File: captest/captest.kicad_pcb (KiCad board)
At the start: 2 copper layers, 36.2 x 36.2 mm, 12 parts, among them IC1 ATTINY861-P, P1 CONN_2, P2 CONN_6, P3 CONN_3X2

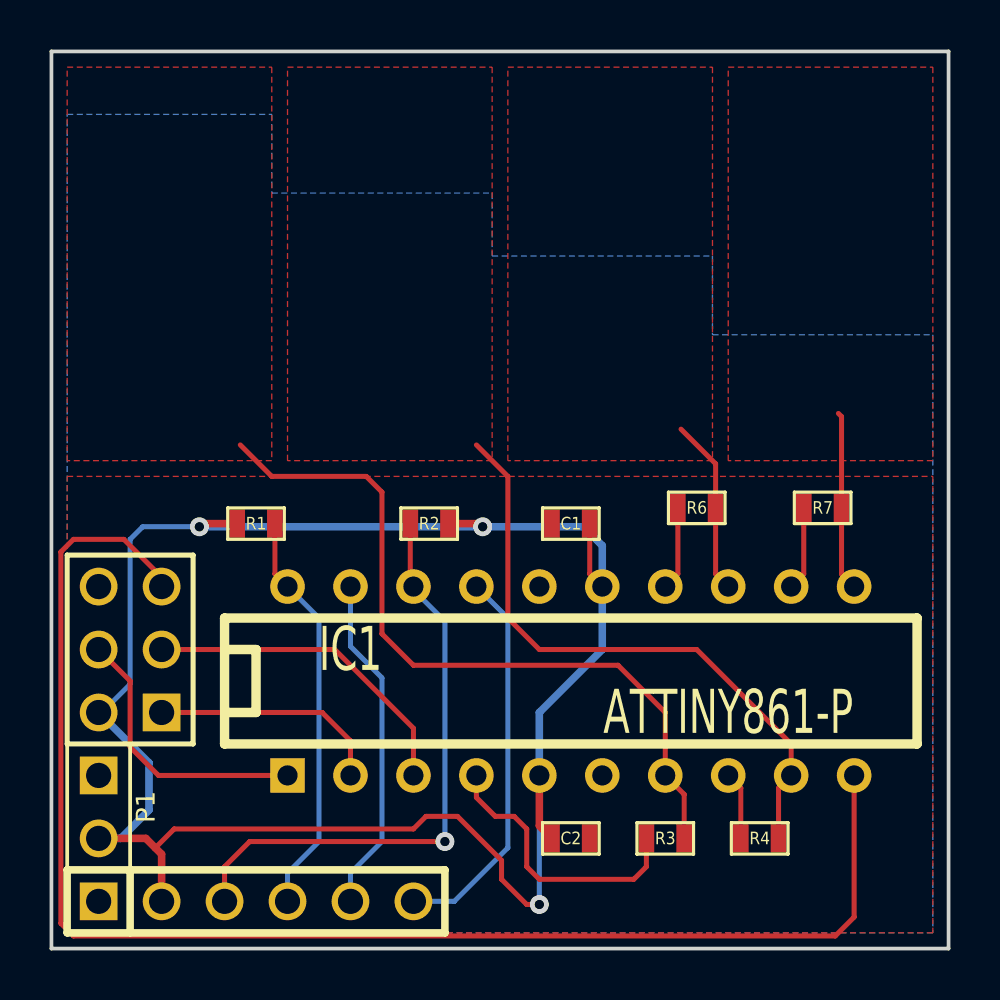
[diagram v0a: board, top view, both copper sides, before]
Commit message: Captest silkscreen adjustments
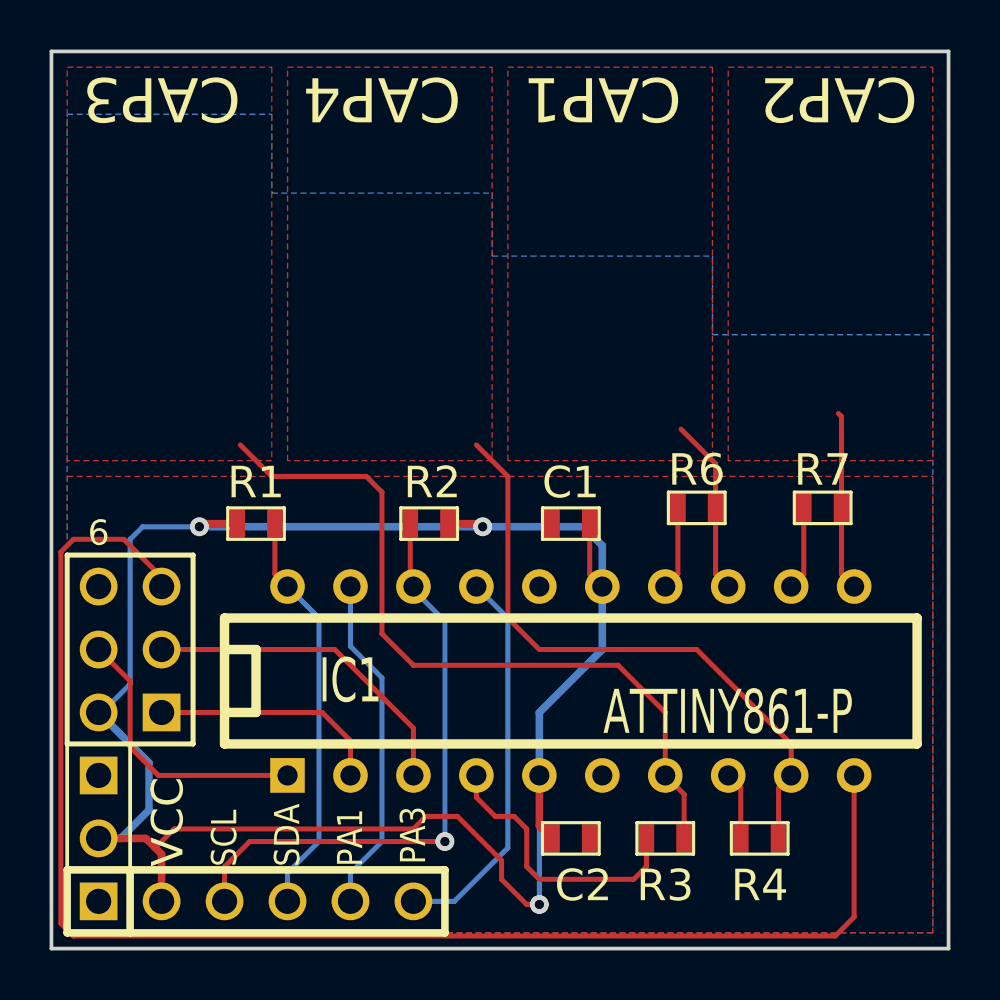
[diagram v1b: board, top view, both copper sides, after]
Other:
- board text added: "6"
- board text added: "CAP1"
- board text added: "CAP2"
- board text added: "CAP3"
- board text added: "CAP4"
- board text added: "Capacitive touch sensor test board"
- board text added: "PA1"
- board text added: "PA3"
- board text added: "SCL"
- board text added: "SDA"
- board text added: "VCC"

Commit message: Captest updates
* Change to SOIC-20 version of ATtiny861
* Add filtering caps on sense pins
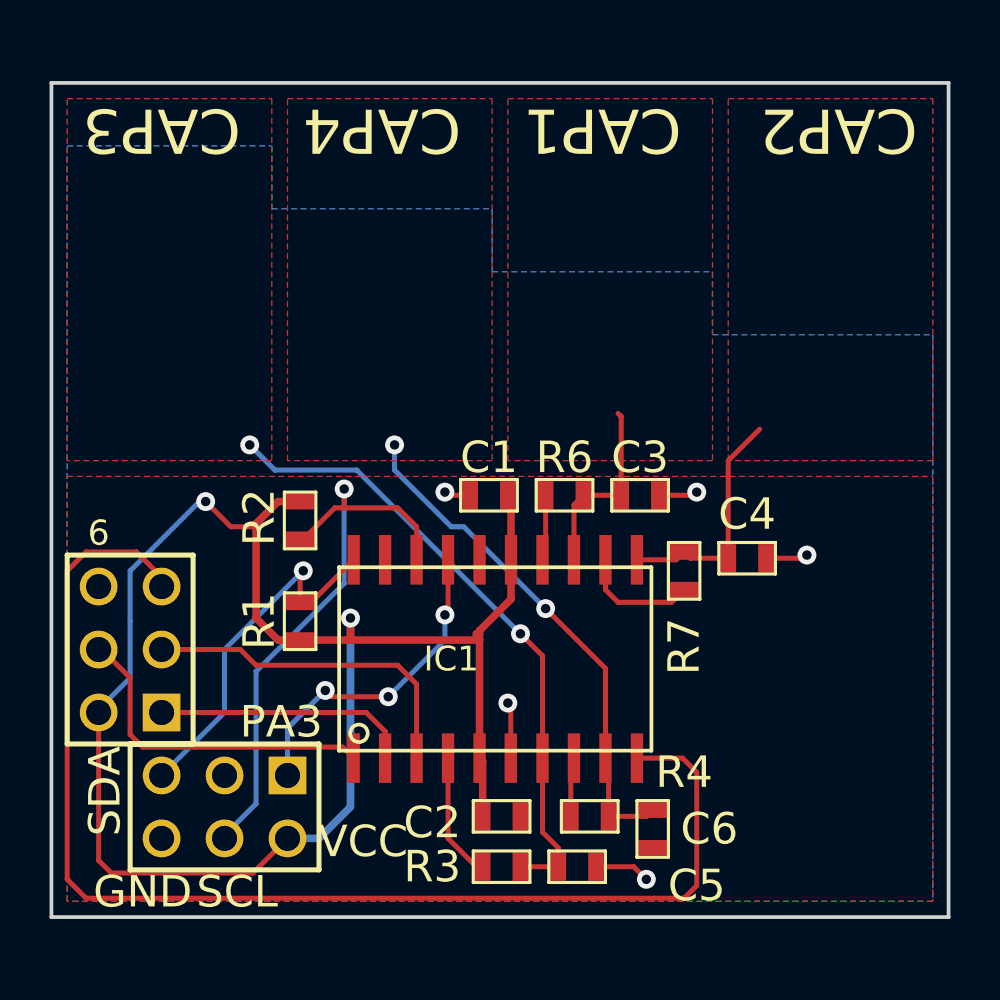
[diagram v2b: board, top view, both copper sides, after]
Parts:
- removed P2: CONN_6, PIN_ARRAY-6X1
- added C3: C, SM0603, F.Cu at (162.8, 90.9)
- added C4: C, SM0603, F.Cu at (167.1, 93.5)
- added C5: C, SM0603, F.Cu at (160.3, 105.9)
- added C6: C, SM0603, F.Cu at (163.3, 104.4)
- IC1: footprint DIP-20__300 -> SOIC20-7.4MM
- P1: value CONN_2 -> CONN_3X2; footprint PIN_ARRAY_2X1 -> pin_array_3x2
- moved R4 6.92 mm to (160.8, 103.9)
- moved R3 6.70 mm to (157.2, 105.9)
- moved R7 6.14 mm to (164.6, 94.0), turned to 90 degrees
- moved R6 5.36 mm to (159.8, 90.9)
- moved R2 5.21 mm to (149.1, 91.9), turned to 270 degrees
- moved P1 5.08 mm to (146.1, 103.5), turned to 180 degrees
- moved R1 4.32 mm to (149.1, 96.0), turned to 90 degrees
- moved C1 3.49 mm to (156.7, 90.9)
- moved IC1 3.18 mm to (157.0, 97.5)
- moved C2 2.93 mm to (157.2, 103.9)
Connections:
- IC1 pad 19: /PA1 -> (no net)
- P1 pad 1: GND -> /PA3
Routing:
- net /PA1: track 13.8 -> 0.00 mm
- net VCC: track 81.2 -> 68.5 mm, vias 3 -> 2
- net GND: track 0.00 -> 8.86 mm, vias 0 -> 5
- net /nRESET: track 58.5 -> 50.5 mm
- net N-000006: track 11.4 -> 5.11 mm
- net /CAP3: track 30.4 -> 25.6 mm, vias 0 -> 2
- net /CAP4: track 25.1 -> 20.7 mm, vias 0 -> 2
- net /PA3: track 15.8 -> 13.2 mm, vias 0 -> 3
- net /CAP2: track 7.25 -> 9.65 mm
- net /MOSI: track 11.3 -> 13.4 mm
- net /SDA: track 16.5 -> 14.8 mm, vias 0 -> 1
- net N-0000013: track 3.39 -> 4.80 mm
- net /MISO: track 9.49 -> 10.4 mm
- net N-0000014: track 3.39 -> 2.66 mm
- net /CAP1: track 7.14 -> 7.64 mm
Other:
- board size 36.2 x 36.2 mm -> 36.2 x 33.7 mm
- board text added: "GND"
- board text removed: "PA1"

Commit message: Captest update with TSSOP and more density
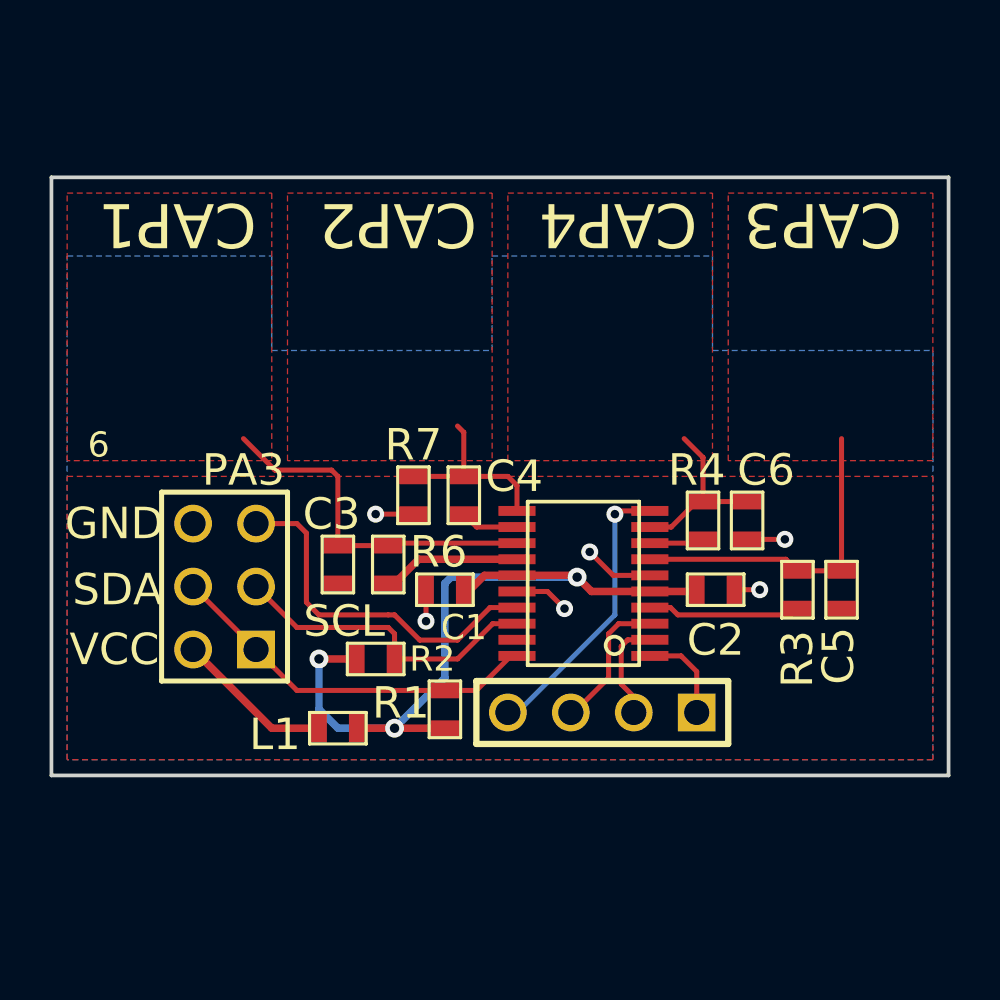
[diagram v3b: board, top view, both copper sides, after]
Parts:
- removed P3: CONN_3X2, pin_array_3x2
- added L1: INDUCTOR, SM0603, F.Cu at (150.6, 100.3)
- added P2: CONN_4, PIN_ARRAY_4x1, F.Cu at (161.3, 99.7)
- IC1: footprint SOIC20-7.4MM -> TSSOP20-4.5MM
- moved R3 16.4 mm to (169.2, 94.7), turned to 90 degrees
- moved C5 15.5 mm to (170.9, 94.7), turned to 270 degrees
- moved C4 13.7 mm to (153.7, 90.9), turned to 270 degrees
- moved C6 13.0 mm to (167.1, 91.9)
- moved R4 12.8 mm to (165.4, 91.9), turned to 90 degrees
- moved C2 12.6 mm to (165.9, 94.7)
- moved C3 12.5 mm to (150.6, 93.7), turned to 270 degrees
- moved R7 9.40 mm to (155.7, 90.9)
- moved P1 8.89 mm to (146.1, 94.6), turned to 90 degrees
- moved R6 7.64 mm to (152.7, 93.7), turned to 90 degrees
- moved R1 6.84 mm to (154.9, 99.6)
- moved R2 6.37 mm to (152.1, 97.5), turned to 0 degrees
- moved IC1 4.68 mm to (160.5, 94.5), turned to 90 degrees
- moved C1 4.20 mm to (154.9, 94.7)
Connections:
- P1 pad 1: /PA3 -> /SDA
- P1 pad 2: VCC -> /PWR
- P1 pad 3: (no net) -> /SCL
- P1 pad 4: /SCL -> /SDA
- P1 pad 5: /SDA -> /PA3
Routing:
- net /nRESET: track 50.5 -> 11.5 mm, vias 0 -> 1
- net VCC: track 68.5 -> 32.6 mm, vias 2 -> 3
- net /CAP4: track 20.7 -> 7.21 mm, vias 2 -> 0
- net /CAP3: track 25.6 -> 13.3 mm, vias 2 -> 0
- net /SCL: track 23.7 -> 12.9 mm, vias 1 -> 0
- net /MOSI: track 13.4 -> 3.80 mm
- net /SCK: track 13.8 -> 5.71 mm
- net /CAP1: track 7.64 -> 14.5 mm
- net /PWR: track 0.00 -> 6.40 mm
- net /MISO: track 10.4 -> 4.14 mm
- net N-000006: track 2.66 -> 5.60 mm
- net N-000002: track 4.80 -> 2.36 mm
- net /CAP2: track 9.65 -> 7.49 mm
- net GND: track 8.86 -> 10.4 mm, vias 5 -> 6
- net /PA3: track 13.2 -> 14.7 mm, vias 3 -> 0
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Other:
- board size 36.2 x 33.7 mm -> 36.2 x 24.1 mm
- net class Default: via_dia 0.762 -> 0.6858; via_drill 0.508 -> 0.381
- board text added: "MISO"
- board text added: "MOSI"
- board text added: "RESET"
- board text added: "SCK"

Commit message: Optimize captest layout
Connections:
- IC1 pad 19: (no net) -> GND
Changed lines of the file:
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@@
 (kicad_pcb (version 3) (host pcbnew "(2013-feb-26)-testing")
   (general
-    (links 37)
+    (links 38)
     (no_connects 0)
     (area 138.989999 78.029999 175.335001 103.0986)
@@
     (user_trace_width 0.2032)
     (trace_clearance 0.2032)
-    (zone_clearance 0.2032)
+    (zone_clearance 0.254)
     (zone_45_only no)
     (trace_min 0.1524)
@@
   (net 14 N-000001)
   (net 15 N-000002)
-  (net 16 N-000006)
-  (net 17 N-000007)
+  (net 16 N-000004)
+  (net 17 N-000005)
   (net 18 VCC)
   (net_class Default "This is the default net class."
@@
     (add_net N-000001)
     (add_net N-000002)
-    (add_net N-000006)
-    (add_net N-000007)
+    (add_net N-000004)
+    (add_net N-000005)
   )
   (net_class power ""
@@
     (pad 1 smd rect (at -0.762 0 90) (size 0.635 1.143)
       (layers F.Cu F.Paste F.Mask)
-      (net 16 N-000006)
+      (net 16 N-000004)
     )
     (pad 2 smd rect (at 0.762 0 90) (size 0.635 1.143)
@@
     (pad 1 smd rect (at -0.762 0 90) (size 0.635 1.143)
       (layers F.Cu F.Paste F.Mask)
-      (net 15 N-000002)
+      (net 17 N-000005)
     )
     (pad 2 smd rect (at 0.762 0 90) (size 0.635 1.143)
@@
     (pad 1 smd rect (at -0.762 0 90) (size 0.635 1.143)
       (layers F.Cu F.Paste F.Mask)
-      (net 17 N-000007)
+      (net 15 N-000002)
     )
     (pad 2 smd rect (at 0.762 0 90) (size 0.635 1.143)
@@
     (pad 8 smd rect (at 1.625 2.68 90) (size 0.4 1.5)
       (layers F.Cu F.Paste F.Mask)
-      (net 17 N-000007)
+      (net 15 N-000002)
       (clearance 0.125)
     )
@@
     (pad 12 smd rect (at 2.275 -2.68 90) (size 0.4 1.5)
       (layers F.Cu F.Paste F.Mask)
-      (net 15 N-000002)
+      (net 17 N-000005)
       (clearance 0.125)
     )
@@
     (pad 14 smd rect (at 0.975 -2.68 90) (size 0.4 1.5)
       (layers F.Cu F.Paste F.Mask)
-      (net 16 N-000006)
+      (net 16 N-000004)
       (clearance 0.125)
     )
@@
     (pad 19 smd rect (at -2.275 -2.68 90) (size 0.4 1.5)
       (layers F.Cu F.Paste F.Mask)
+      (net 13 GND)
       (clearance 0.125)
     )
@@
   (segment (start 164.338 95.758) (end 168.91 95.758) (width 0.2032) (layer F.Cu) (net 14))
   (segment (start 164.043 95.463) (end 164.338 95.758) (width 0.2032) (layer F.Cu) (net 14))
-  (segment (start 157.848 92.213) (end 156.221 92.213) (width 0.2032) (layer F.Cu) (net 15))
-  (segment (start 156.221 92.213) (end 155.702 91.694) (width 0.2032) (layer F.Cu) (net 15))
+  (segment (start 163.208 92.863) (end 165.201 92.863) (width 0.2032) (layer F.Cu) (net 15))
+  (segment (start 165.201 92.863) (end 165.354 92.71) (width 0.2032) (layer F.Cu) (net 15))
   (segment (start 152.654 94.488) (end 152.908 94.488) (width 0.3048) (layer F.Cu) (net 16))
   (segment (start 153.883 93.513) (end 157.848 93.513) (width 0.3048) (layer F.Cu) (net 16))
   (segment (start 152.908 94.488) (end 153.883 93.513) (width 0.3048) (layer F.Cu) (net 16))
-  (segment (start 163.208 92.863) (end 165.201 92.863) (width 0.2032) (layer F.Cu) (net 17))
-  (segment (start 165.201 92.863) (end 165.354 92.71) (width 0.2032) (layer F.Cu) (net 17))
+  (segment (start 157.848 92.213) (end 156.221 92.213) (width 0.2032) (layer F.Cu) (net 17))
+  (segment (start 156.221 92.213) (end 155.702 91.694) (width 0.2032) (layer F.Cu) (net 17))
   (segment (start 151.384 97.536) (end 149.86 97.536) (width 0.3048) (layer F.Cu) (net 18))
   (segment (start 150.622 100.33) (end 152.908 100.33) (width 0.3048) (layer B.Cu) (net 18))
@@
     )
   )
-  (zone (net 3) (net_name /CAP3) (layer F.Cu) (hatch edge 0.508)
+  (zone (net 1) (net_name /CAP1) (layer F.Cu) (hatch edge 0.508)
     (connect_pads (clearance 0.254))
     (min_thickness 0.254)
@@
     )
   )
-  (zone (net 4) (net_name /CAP4) (layer F.Cu) (hatch edge 0.508)
+  (zone (net 2) (net_name /CAP2) (layer F.Cu) (hatch edge 0.508)
     (connect_pads (clearance 0.254))
     (min_thickness 0.254)
@@
     )
   )
-  (zone (net 1) (net_name /CAP1) (layer F.Cu) (hatch edge 0.508)
+  (zone (net 4) (net_name /CAP4) (layer F.Cu) (hatch edge 0.508)
     (connect_pads (clearance 0.254))
     (min_thickness 0.254)
@@
     )
   )
-  (zone (net 2) (net_name /CAP2) (layer F.Cu) (hatch edge 0.508)
+  (zone (net 3) (net_name /CAP3) (layer F.Cu) (hatch edge 0.508)
     (connect_pads (clearance 0.254))
     (min_thickness 0.254)

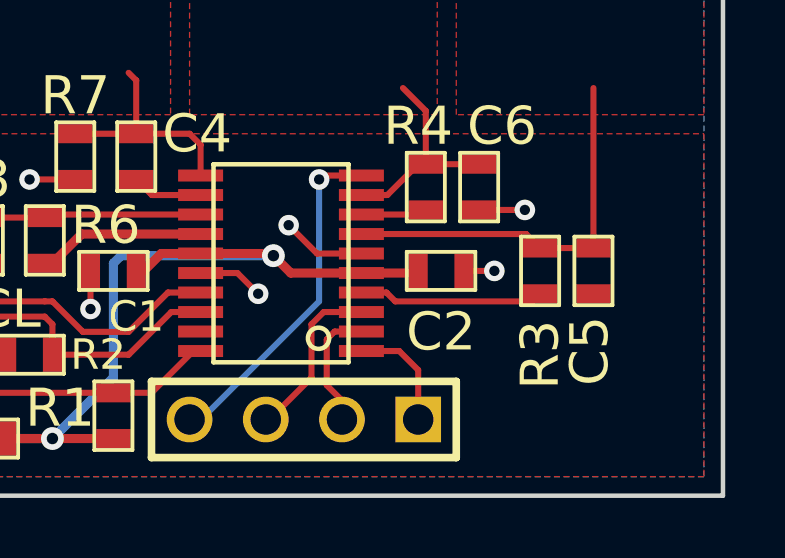
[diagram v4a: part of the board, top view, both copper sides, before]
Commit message: Better routing of ground pour around ATtiny861 main bypass cap
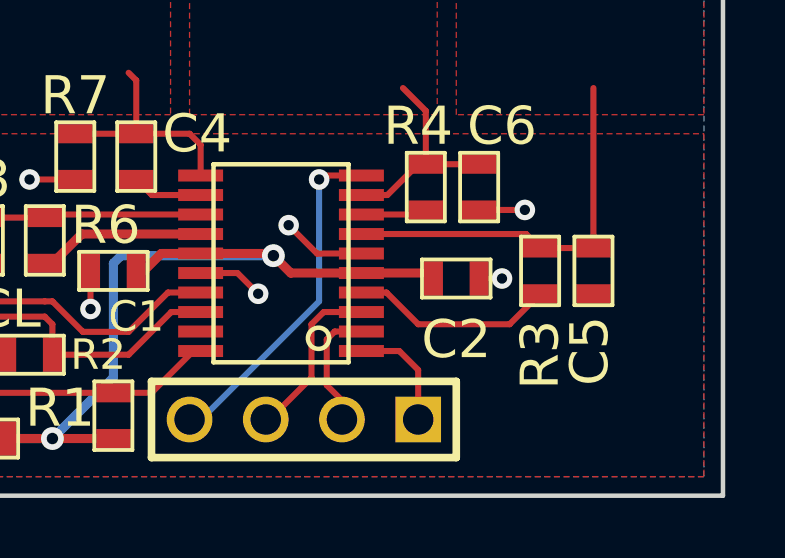
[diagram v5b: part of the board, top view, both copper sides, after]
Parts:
- moved C2 0.57 mm to (166.4, 95.0)
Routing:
- net N-000001: track 6.18 -> 6.81 mm
- net VCC: track 32.6 -> 33.2 mm
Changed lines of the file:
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@@
-(kicad_pcb (version 3) (host pcbnew "(2013-feb-26)-testing")
+(kicad_pcb (version 3) (host pcbnew "(2013-mar-08)-testing")
   (general
     (links 38)
@@
   )
   (module SM0603 (layer F.Cu)
-    (at 165.862 94.742)
+    (at 166.37 94.996)
     (attr smd)
     (fp_text reference C2 (at 0 2.032) (layer F.SilkS)
@@
   (segment (start 161.798 95.758) (end 161.798 91.694) (width 0.2032) (layer B.Cu) (net 12))
   (segment (start 157.861 99.695) (end 161.798 95.758) (width 0.2032) (layer B.Cu) (net 12))
+  (segment (start 167.132 94.996) (end 167.894 94.996) (width 0.2032) (layer F.Cu) (net 13))
+  (via (at 167.894 94.996) (size 0.6858) (layers F.Cu B.Cu) (net 13))
   (segment (start 154.178 94.742) (end 154.178 96.012) (width 0.2032) (layer F.Cu) (net 13))
   (via (at 154.178 96.012) (size 0.6858) (layers F.Cu B.Cu) (net 13))
@@
   (via (at 160.782 93.218) (size 0.6858) (layers F.Cu B.Cu) (net 13))
   (segment (start 161.727 94.163) (end 160.782 93.218) (width 0.2032) (layer F.Cu) (net 13))
-  (segment (start 166.624 94.742) (end 167.64 94.742) (width 0.2032) (layer F.Cu) (net 13))
-  (via (at 167.64 94.742) (size 0.6858) (layers F.Cu B.Cu) (net 13))
   (segment (start 167.132 92.71) (end 168.656 92.71) (width 0.2032) (layer F.Cu) (net 13))
   (via (at 168.656 92.71) (size 0.6858) (layers F.Cu B.Cu) (net 13))
   (segment (start 163.208 95.463) (end 164.043 95.463) (width 0.2032) (layer F.Cu) (net 14))
-  (segment (start 168.91 95.758) (end 169.164 95.504) (width 0.2032) (layer F.Cu) (net 14))
-  (segment (start 164.338 95.758) (end 168.91 95.758) (width 0.2032) (layer F.Cu) (net 14))
-  (segment (start 164.043 95.463) (end 164.338 95.758) (width 0.2032) (layer F.Cu) (net 14))
+  (segment (start 168.148 96.52) (end 169.164 95.504) (width 0.2032) (layer F.Cu) (net 14))
+  (segment (start 165.1 96.52) (end 168.148 96.52) (width 0.2032) (layer F.Cu) (net 14))
+  (segment (start 164.043 95.463) (end 165.1 96.52) (width 0.2032) (layer F.Cu) (net 14))
   (segment (start 163.208 92.863) (end 165.201 92.863) (width 0.2032) (layer F.Cu) (net 15))
   (segment (start 165.201 92.863) (end 165.354 92.71) (width 0.2032) (layer F.Cu) (net 15))
@@
   (segment (start 157.848 92.213) (end 156.221 92.213) (width 0.2032) (layer F.Cu) (net 17))
   (segment (start 156.221 92.213) (end 155.702 91.694) (width 0.2032) (layer F.Cu) (net 17))
+  (segment (start 163.208 94.813) (end 165.425 94.813) (width 0.3048) (layer F.Cu) (net 18))
+  (segment (start 165.425 94.813) (end 165.608 94.996) (width 0.3048) (layer F.Cu) (net 18))
   (segment (start 151.384 97.536) (end 149.86 97.536) (width 0.3048) (layer F.Cu) (net 18))
   (segment (start 150.622 100.33) (end 152.908 100.33) (width 0.3048) (layer B.Cu) (net 18))
@@
   (segment (start 160.853 94.813) (end 163.208 94.813) (width 0.3048) (layer F.Cu) (net 18))
   (segment (start 160.203 94.163) (end 160.853 94.813) (width 0.3048) (layer F.Cu) (net 18))
-  (segment (start 163.208 94.813) (end 165.029 94.813) (width 0.3048) (layer F.Cu) (net 18))
-  (segment (start 165.029 94.813) (end 165.1 94.742) (width 0.3048) (layer F.Cu) (net 18))
   (zone (net 13) (net_name GND) (layer B.Cu) (hatch edge 0.508)
     (connect_pads (clearance 0.254))
